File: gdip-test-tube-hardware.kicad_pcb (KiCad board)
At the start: 2 copper layers, 76.2 x 58.5 mm, 44 parts, among them J1 USB_B, J2 USB_B, J3 Conn_01x06, J4 Conn_01x06, J5 Conn_01x06, J6 Screw_Terminal_01x02, Q1 BC818, Q3 BC818, SW1 SW_Push, SW2 SW_Push, U1 ESP32-S3-WROOM-1-N16R2, U2 AMS1117-3.3, U3 CP2102N-Axx-xQFN28, U4 USBLC6-2SC6, U5 USBLC6-2SC6

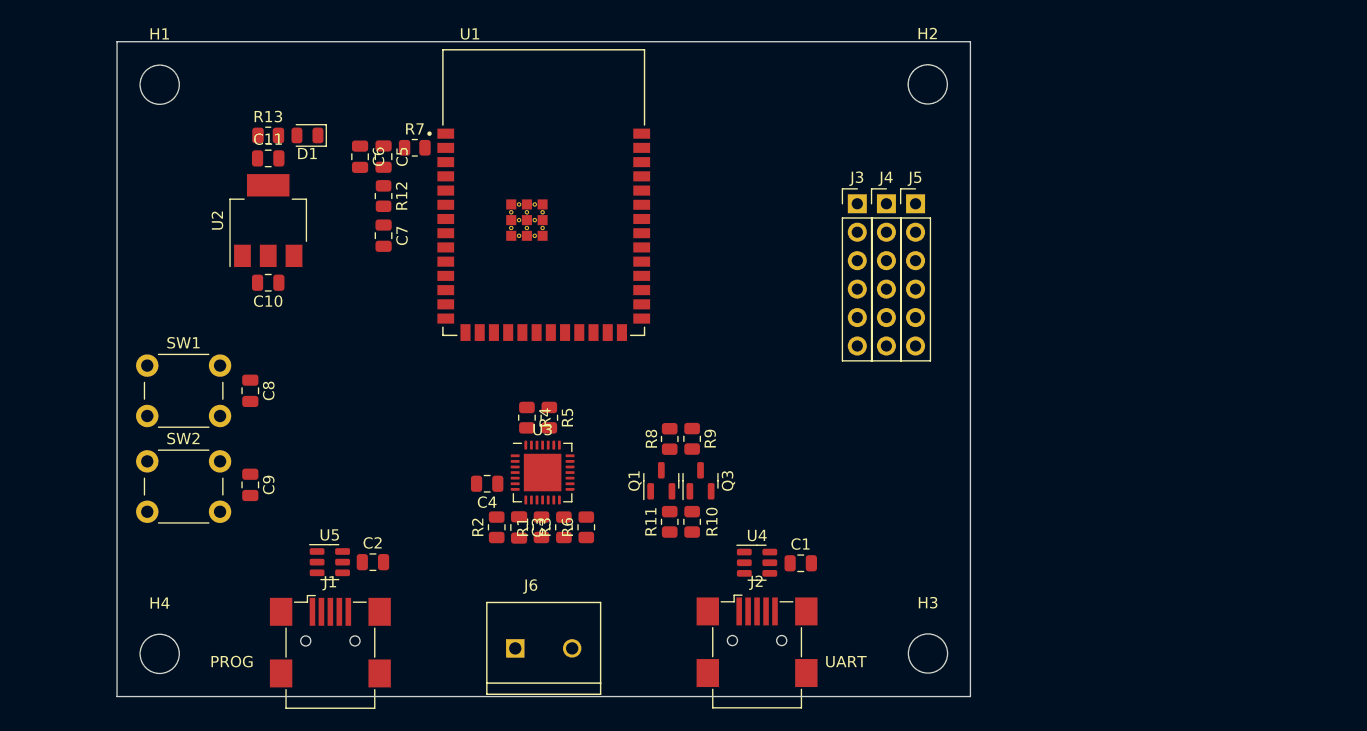
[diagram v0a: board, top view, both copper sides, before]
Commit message: Added buzzer circuit in.
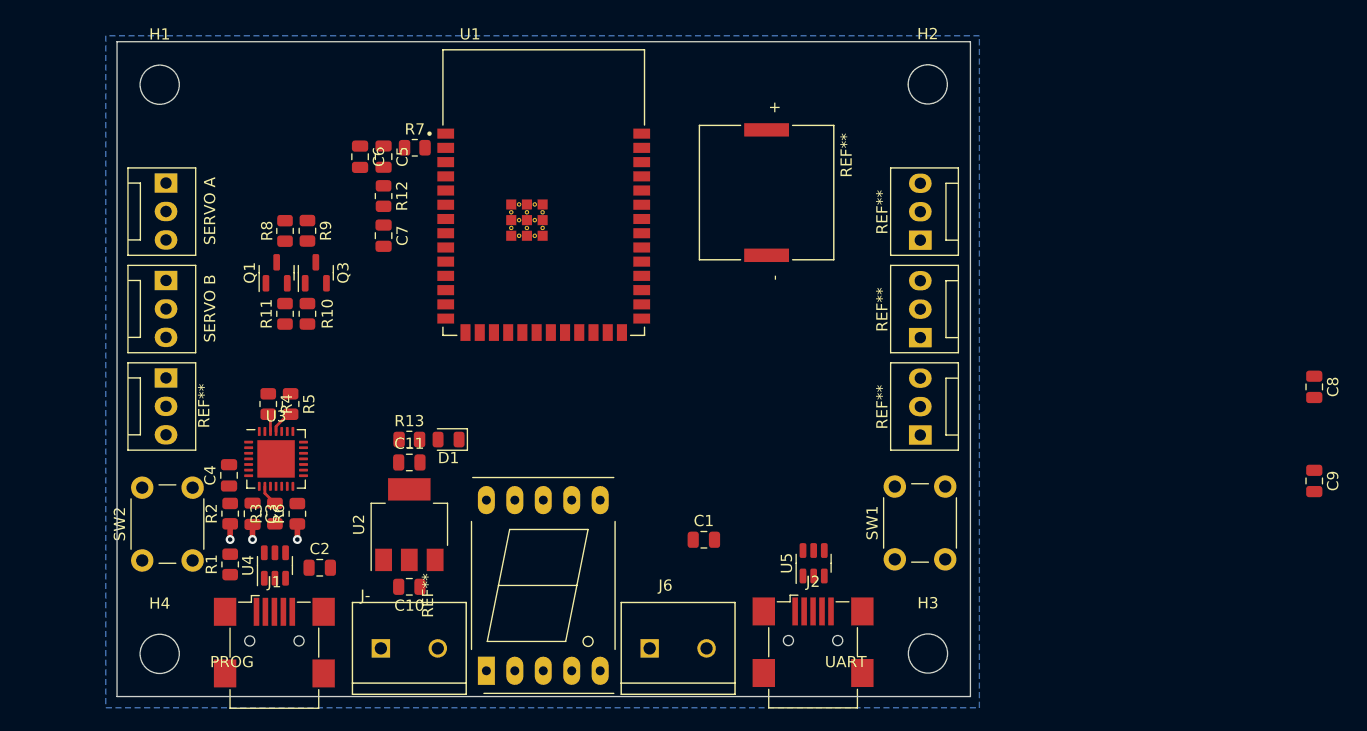
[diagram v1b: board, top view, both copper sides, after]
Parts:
- removed J3, J4, J5: Conn_01x06, Connector_PinHeader_2.54mm:PinHeader_1x06_P2.54mm_Vertical
- added J-: Screw_Terminal_01x02, gdip-test-tube:TE_282837-2, F.Cu at (126.1, 133.7)
- added REF**: FanPinHeader_1x03_P2.54mm_Vertical, Connector:FanPinHeader_1x03_P2.54mm_Vertical, F.Cu at (171.7, 106.0)
- added REF**: SPKR_PKLCS1212E40A1-R1, gdip-test-tube:SPKR_PKLCS1212E40A1-R1, F.Cu at (158.0, 93.0)
- added REF**: 7SegmentLED_LTS6760_LTS6780, Display_7Segment:7SegmentLED_LTS6760_LTS6780, F.Cu at (133.0, 135.7)
- added REF**: FanPinHeader_1x03_P2.54mm_Vertical, Connector:FanPinHeader_1x03_P2.54mm_Vertical, F.Cu at (171.7, 97.2)
- added REF**: FanPinHeader_1x03_P2.54mm_Vertical, Connector:FanPinHeader_1x03_P2.54mm_Vertical, F.Cu at (104.4, 109.5)
- added REF**: FanPinHeader_1x03_P2.54mm_Vertical, Connector:FanPinHeader_1x03_P2.54mm_Vertical, F.Cu at (171.7, 114.7)
- added SERVO A: FanPinHeader_1x03_P2.54mm_Vertical, Connector:FanPinHeader_1x03_P2.54mm_Vertical, F.Cu at (104.4, 92.2)
- added SERVO B: FanPinHeader_1x03_P2.54mm_Vertical, Connector:FanPinHeader_1x03_P2.54mm_Vertical, F.Cu at (104.4, 100.8)
- moved C8 95.0 mm to (206.9, 110.3)
- moved C9 95.0 mm to (206.9, 118.8)
- moved SW1 69.0 mm to (169.4, 125.8), turned to 90 degrees
- moved U5 43.2 mm to (162.2, 126.1), turned to 90 degrees
- moved U4 43.1 mm to (114.1, 126.3), turned to 90 degrees
- moved Q1 39.1 mm to (114.2, 100.2)
- moved Q3 39.1 mm to (117.8, 100.2)
- moved R10 39.1 mm to (117.0, 103.8)
- moved R11 39.1 mm to (115.0, 103.8)
- moved R8 39.1 mm to (115.0, 96.4)
- moved R9 39.1 mm to (117.0, 96.4)
- moved U2 29.9 mm to (126.1, 122.7)
- moved C10 29.9 mm to (126.1, 128.2)
- moved C11 29.9 mm to (126.1, 117.1)
- moved D1 29.9 mm to (129.6, 115.0)
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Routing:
- net GND: track 0.00 -> 4.14 mm, vias 0 -> 3
- net Net-(U3-RXD): track 0.00 -> 2.20 mm
- net Net-(U3-~{RST}): track 0.00 -> 1.90 mm
- net Net-(U3-TXD): track 0.00 -> 1.62 mm
- added copper zone on B.Cu, net GND

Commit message: Removed multiplexer for buzzer and servo as we can remap any ESP32 pin. Also switched mux for shift register for the 7-seg display.
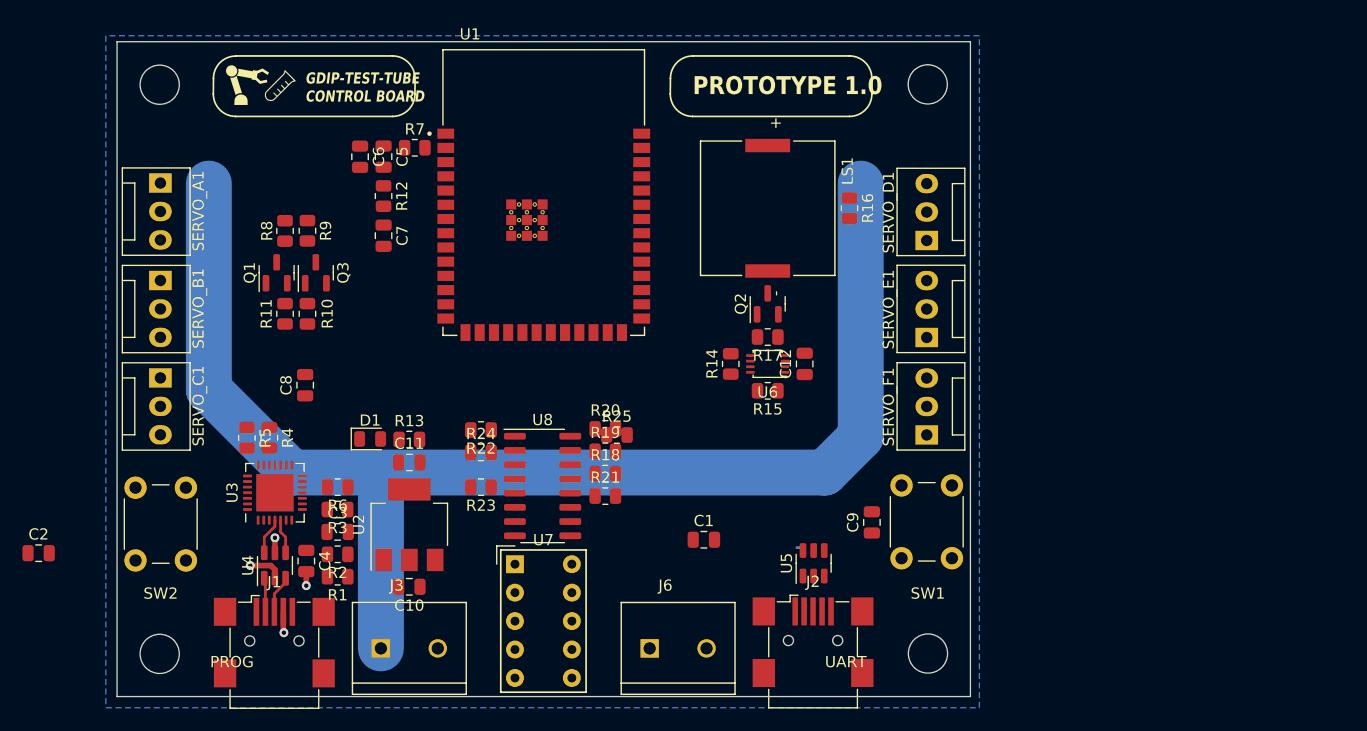
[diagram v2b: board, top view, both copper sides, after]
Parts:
- removed J-: Screw_Terminal_01x02, gdip-test-tube:TE_282837-2
- removed REF** (x4): FanPinHeader_1x03_P2.54mm_Vertical, Connector:FanPinHeader_1x03_P2.54mm_Vertical
- removed REF**: SPKR_PKLCS1212E40A1-R1, gdip-test-tube:SPKR_PKLCS1212E40A1-R1
- removed REF**: 7SegmentLED_LTS6760_LTS6780, Display_7Segment:7SegmentLED_LTS6760_LTS6780
- removed SERVO A: FanPinHeader_1x03_P2.54mm_Vertical, Connector:FanPinHeader_1x03_P2.54mm_Vertical
- removed SERVO B: FanPinHeader_1x03_P2.54mm_Vertical, Connector:FanPinHeader_1x03_P2.54mm_Vertical
- added C12: 0.001uF, Capacitor_SMD:C_0805_2012Metric, F.Cu at (161.4, 108.3)
- added G***: LOGO, LOGO, F.Cu at (114.2, 83.4)
- added G***: LOGO, LOGO, F.Cu at (111.6, 83.4)
- added J3: Screw_Terminal_01x02, gdip-test-tube:TE_282837-2, F.Cu at (126.1, 133.7)
- added LS1: PKLCS1212E40A1-R1, gdip-test-tube:SPKR_PKLCS1212E40A1-R1, F.Cu at (158.1, 94.4)
- added Q2: BC818, Package_TO_SOT_SMD:SOT-23, F.Cu at (158.1, 102.9)
- added R14: 120K, Resistor_SMD:R_0805_2012Metric, F.Cu at (154.8, 108.3)
- added R15: 1M, Resistor_SMD:R_0805_2012Metric, F.Cu at (158.1, 110.7)
- added R16: 1K, Resistor_SMD:R_0805_2012Metric, F.Cu at (165.4, 94.4)
- added R17: 1K, Resistor_SMD:R_0805_2012Metric, F.Cu at (158.1, 105.9)
- added R18: 330, Resistor_SMD:R_0805_2012Metric, F.Cu at (143.6, 118.1)
- added R19: 330, Resistor_SMD:R_0805_2012Metric, F.Cu at (143.6, 116.1)
- added R20: 330, Resistor_SMD:R_0805_2012Metric, F.Cu at (143.6, 114.1)
- added R21: 330, Resistor_SMD:R_0805_2012Metric, F.Cu at (143.6, 120.1)
- added R22: 330, Resistor_SMD:R_0805_2012Metric, F.Cu at (132.5, 114.2)
- added R23: 330, Resistor_SMD:R_0805_2012Metric, F.Cu at (132.5, 119.3)
- added R24: 330, Resistor_SMD:R_0805_2012Metric, F.Cu at (132.5, 116.2)
- added R25: 330, Resistor_SMD:R_0805_2012Metric, F.Cu at (144.6, 114.7)
- added SERVO_A1: Conn_01x03_Pin, Connector:FanPinHeader_1x03_P2.54mm_Vertical, F.Cu at (103.9, 92.2)
- added SERVO_B1: Conn_01x03_Pin, Connector:FanPinHeader_1x03_P2.54mm_Vertical, F.Cu at (103.9, 100.8)
- added SERVO_C1: Conn_01x03_Pin, Connector:FanPinHeader_1x03_P2.54mm_Vertical, F.Cu at (103.9, 109.5)
- added SERVO_D1: Conn_01x03_Pin, Connector:FanPinHeader_1x03_P2.54mm_Vertical, F.Cu at (172.3, 97.3)
- added SERVO_E1: Conn_01x03_Pin, Connector:FanPinHeader_1x03_P2.54mm_Vertical, F.Cu at (172.3, 105.9)
- added SERVO_F1: Conn_01x03_Pin, Connector:FanPinHeader_1x03_P2.54mm_Vertical, F.Cu at (172.3, 114.6)
- added U6: 74LVC2G00, Package_SO:VSSOP-8_2.4x2.1mm_P0.5mm, F.Cu at (158.1, 108.3)
- added U7: HDSP-7401, Display_7Segment:HDSP-7401, F.Cu at (135.5, 126.2)
- added U8: 74AHC595, Package_SO:SOIC-16_3.9x9.9mm_P1.27mm, F.Cu at (138.0, 119.2)
- moved C8 90.1 mm to (116.8, 110.2), turned to 90 degrees
- moved C9 39.7 mm to (167.4, 122.5), turned to 90 degrees
- moved C2 25.1 mm to (93.0, 125.2)
- moved C4 10.3 mm to (116.9, 125.9), turned to -90 degrees
- moved R2 10.3 mm to (119.7, 125.3), turned to 180 degrees
- moved R1 9.66 mm to (119.7, 127.3), turned to 180 degrees
- moved C3 7.77 mm to (119.7, 123.3), turned to 0 degrees
- moved D1 7.00 mm to (122.6, 115.0), turned to 0 degrees
- moved R3 5.60 mm to (119.7, 121.3), turned to 180 degrees
- moved R5 4.93 mm to (111.6, 114.9)
- moved R6 4.32 mm to (119.7, 119.3), turned to 180 degrees
- moved R4 3.02 mm to (113.6, 114.9)
- moved U3 3.02 mm to (114.1, 119.8), turned to 90 degrees
- moved SW1 0.61 mm to (170.1, 125.7)
- moved SW2 0.60 mm to (101.7, 125.8)
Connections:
- J6 pad 1: +5V -> unconnected-(J6-Pin_1-Pad1)
- J6 pad 2: GND -> unconnected-(J6-Pin_2-Pad2)
- U1 pad 12: unconnected-(U1-IO8-Pad12) -> /PWMX
- U1 pad 17: unconnected-(U1-IO9-Pad17) -> /PWM6
- U1 pad 18: unconnected-(U1-IO10-Pad18) -> /GPIO_SR_DATA
- U1 pad 19: unconnected-(U1-IO11-Pad19) -> /GPIO_SR_CLOCK
- U1 pad 20: unconnected-(U1-IO12-Pad20) -> /GPIO_SR_RCLK
- U3 pad 4: /D2+_OUT -> /D1+_OUT
- U3 pad 5: /D2-_OUT -> /D1-_OUT
- U4 pad 1: /D1-_IN -> /D1+_IN
- U4 pad 3: /D1+_IN -> /D1-_IN
- U4 pad 4: /D1+_OUT -> /D1-_OUT
- U4 pad 6: /D1-_OUT -> /D1+_OUT
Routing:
- net +5V: track 0.00 -> 120.7 mm, vias 0 -> 1
- net /D1+_IN: track 0.00 -> 3.41 mm
- net /D1+_OUT: track 0.00 -> 3.31 mm
- net /D1-_OUT: track 0.00 -> 3.10 mm
- net /D1-_IN: track 0.00 -> 3.04 mm
- net Net-(U3-RXD): track 2.20 -> 0.00 mm
- net GND: track 4.14 -> 6.25 mm
- net Net-(U3-~{RST}): track 1.90 -> 0.00 mm
- net Net-(U3-TXD): track 1.62 -> 0.00 mm
- net (no net): track 0.00 -> 0.78 mm
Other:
- board text added: "GDIP-TEST-TUBE CONTROL BOARD"
- board text added: "PROTOTYPE 1.0"

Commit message: Further work on layout.
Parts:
- moved C9 58.4 mm to (109.0, 122.7)
- moved C8 51.8 mm to (167.1, 122.4)
- moved C2 18.3 mm to (111.3, 126.2), turned to -90 degrees
- moved R19 13.6 mm to (131.0, 121.2), turned to -90 degrees
- moved R20 12.8 mm to (133.0, 121.2), turned to -90 degrees
- moved R24 11.6 mm to (143.0, 121.2), turned to -90 degrees
- moved C12 10.9 mm to (160.6, 119.1)
- moved R25 10.1 mm to (137.0, 121.2), turned to -90 degrees
- moved R14 10.1 mm to (154.0, 118.3)
- moved U6 10.1 mm to (157.3, 118.3)
- moved R16 10.1 mm to (164.6, 104.4)
- moved LS1 10.1 mm to (157.3, 104.4)
- moved Q2 10.1 mm to (157.3, 113.0)
- moved R15 10.1 mm to (157.3, 120.7), turned to 0 degrees
- moved R17 10.1 mm to (157.3, 115.9)
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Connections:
- SERVO_A1 pad 1: +5V -> /PWM2
- SERVO_A1 pad 2: /PWM1 -> +5V
- SERVO_B1 pad 1: +5V -> /PWM3
- SERVO_B1 pad 2: /PWM2 -> +5V
- SERVO_C1 pad 1: +5V -> /PWM4
- SERVO_C1 pad 2: /PWM3 -> +5V
- SERVO_D1 pad 1: +5V -> /PWM1
- SERVO_D1 pad 2: /PWM4 -> +5V
- SERVO_E1 pad 1: +5V -> /PWM5
- SERVO_E1 pad 2: /PWM5 -> +5V
- SERVO_F1 pad 1: +5V -> /PWMX
- SERVO_F1 pad 2: /PWMX -> +5V
- U1 pad 12: /PWMX -> unconnected-(U1-IO8-Pad12)
- U1 pad 19: /GPIO_SR_CLOCK -> /GPIO_SR_RCLK
- U1 pad 20: /GPIO_SR_RCLK -> /GPIO_SR_CLOCK
- U1 pad 34: unconnected-(U1-IO41-Pad34) -> /PWMX
- U1 pad 35: unconnected-(U1-IO42-Pad35) -> /PWM5
- U1 pad 7: /PWM5 -> unconnected-(U1-IO7-Pad7)
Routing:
- net /U0TXD: track 0.00 -> 63.7 mm
- net /U0RXD: track 0.00 -> 58.5 mm
- net +3.3V: track 0.00 -> 54.3 mm, vias 0 -> 2
- net /GPIO0: track 0.00 -> 42.7 mm
- net /PWM4: track 0.00 -> 39.5 mm, vias 0 -> 2
- net /PWMX: track 0.00 -> 39.5 mm, vias 0 -> 2
- net /PWM3: track 0.00 -> 32.8 mm, vias 0 -> 2
- net /PWM5: track 0.00 -> 32.4 mm, vias 0 -> 2
- net /CHIP_PU: track 0.00 -> 32.0 mm
- net /RTS: track 0.00 -> 29.0 mm, vias 0 -> 2
- net /PWM1: track 0.00 -> 28.3 mm
- net /DTR: track 0.00 -> 27.5 mm
- net /PWM2: track 0.00 -> 27.2 mm, vias 0 -> 2
- net GND: track 6.25 -> 30.5 mm, vias 3 -> 4
- net Net-(U8-QA): track 0.00 -> 16.0 mm
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- added copper zone on F.Cu, net +5V
- added copper zone on F.Cu, net GND
